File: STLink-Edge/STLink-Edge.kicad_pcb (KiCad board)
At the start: 2 copper layers, 30 x 15 mm, 2 parts, among them J1 Conn_edge_socket, J2 Conn_STLink

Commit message: edgelink 2.1
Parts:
- removed J2: Conn_STLink, Connector_PinHeader_2.54mm:PinHeader_1x04_P2.54mm_Vertical
- added J3: Conn_STLink2, Connector_PinHeader_2.54mm:PinHeader_1x05_P2.54mm_Vertical, F.Cu at (69.0, 49.4)
- added SW1: SW_Push_SPDT, Connector_PinHeader_2.54mm:PinHeader_1x03_P2.54mm_Vertical, F.Cu at (57.5, 52.0)
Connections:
- net +3.3V renamed /Boot
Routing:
- net +3.3V: track 0.00 -> 13.6 mm
- net +5V: track 0.00 -> 12.6 mm
- net GND: track 9.89 -> 4.39 mm, vias 4 -> 16
- net /Boot: track 13.6 -> 14.8 mm, vias 2 -> 0
- net /SWDIO: track 31.4 -> 32.1 mm
- added copper zone on F.Cu, net GND
- removed copper zone on F.Cu, net /Boot
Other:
- board text added: "+5V"
- board text added: "5V"
- board text added: "STLink-V2 EdgeDebugger 2024.03 v2.1 by Leo"
- board text removed: "STLink-V2 EdgeDebugger 2024.03 v2.0 by Leo"

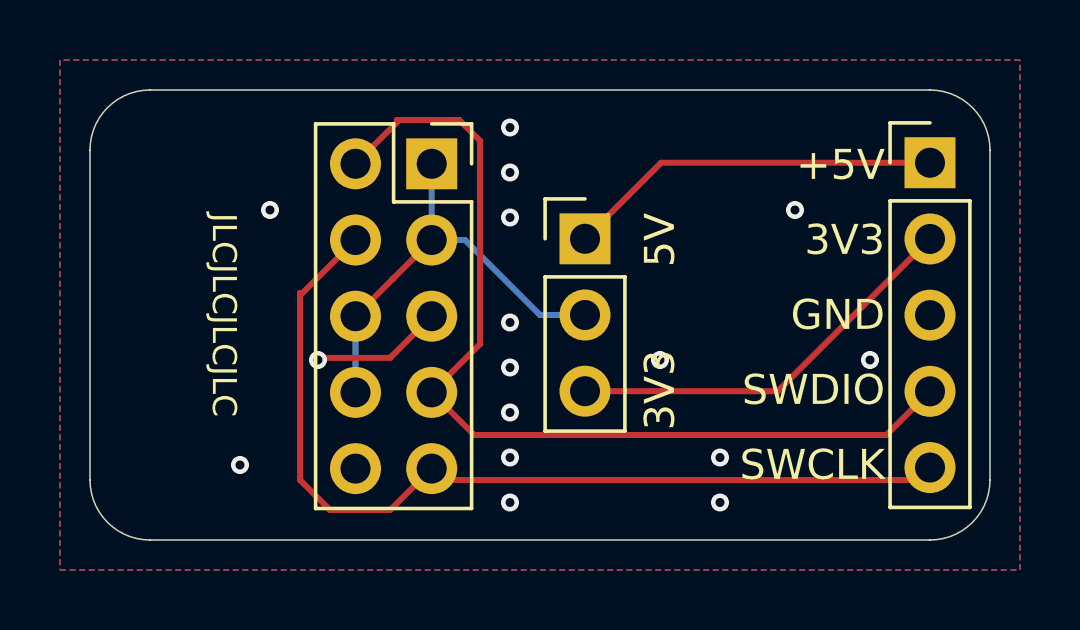
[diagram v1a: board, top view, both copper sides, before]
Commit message: critical fix
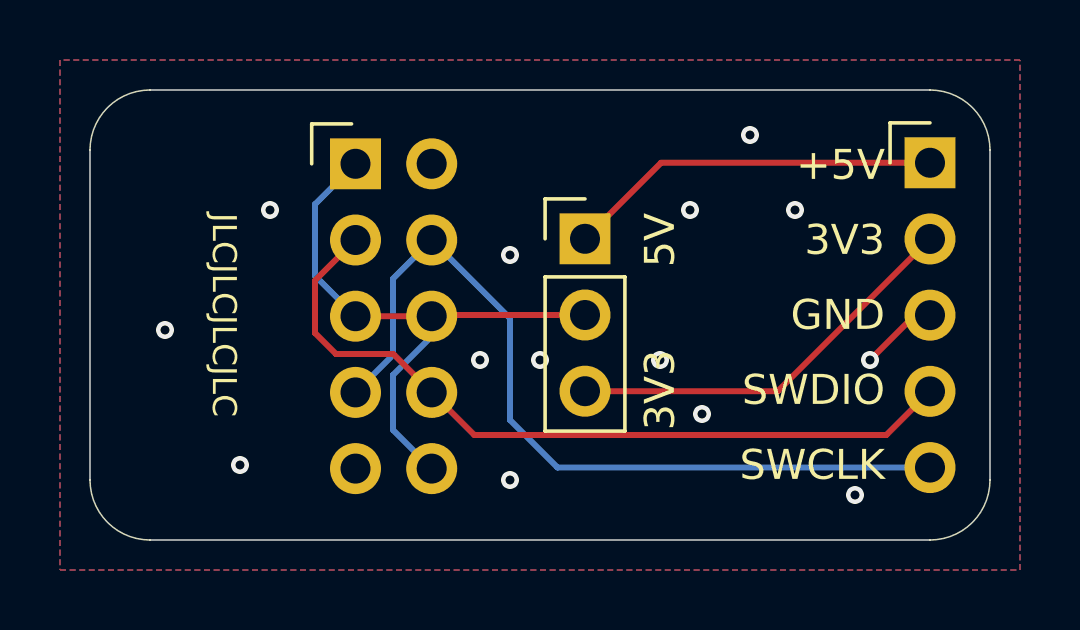
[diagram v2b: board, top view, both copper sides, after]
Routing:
- net /SWDIO: track 32.1 -> 26.3 mm
- net /Boot: track 14.8 -> 20.6 mm
- net /SWCLK: track 31.1 -> 28.5 mm
- net GND: track 4.39 -> 2.62 mm, vias 16 -> 14
